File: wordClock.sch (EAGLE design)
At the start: 29 parts, among them Q1 MOSFET-PCHANNELSMD, Q2 MOSFET-PCHANNELSMD, Q3 MOSFET-PCHANNELSMD, Q4 MOSFET-PCHANNELSMD, Q5 MOSFET-PCHANNELSMD, Q6 MOSFET-PCHANNELSMD, Q7 MOSFET-PCHANNELSMD, Q8 MOSFET-PCHANNELSMD, U1 ATMEGA328P_PDIP, U2 TLC5940-NT

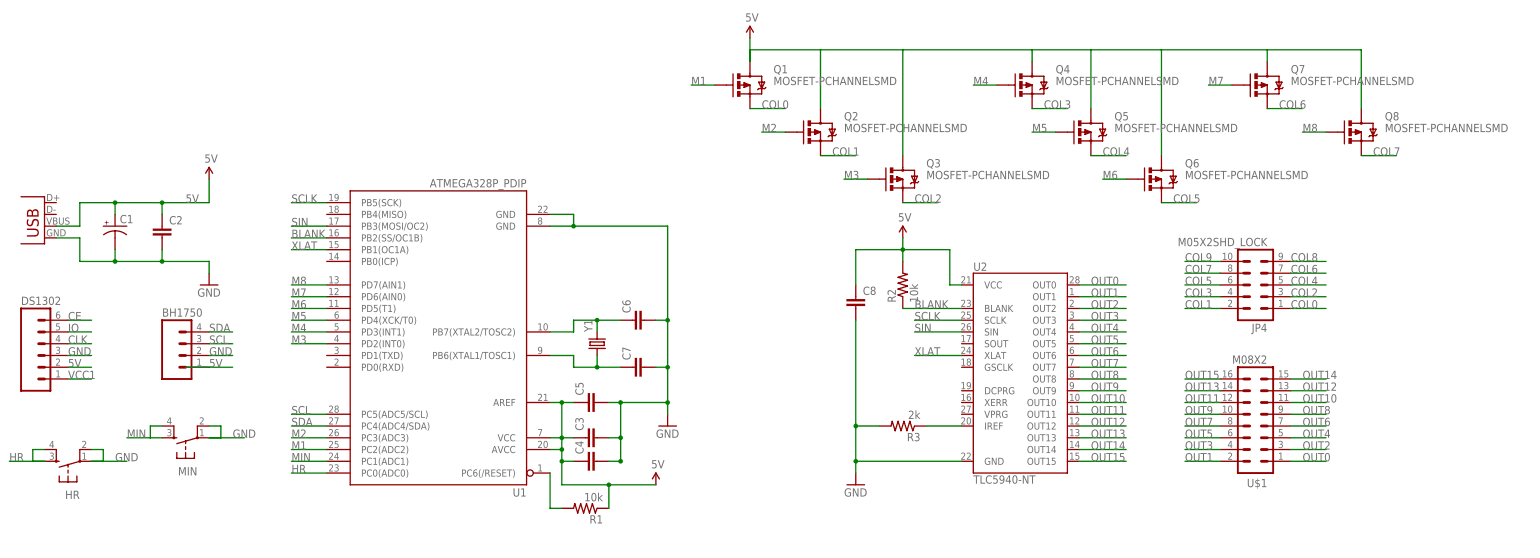
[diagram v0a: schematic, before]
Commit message: added .gitignore, change mosfet layout
Mosfets now occupy one port, for ease of programming. Mosfet D/S are now
flipped the right direction.
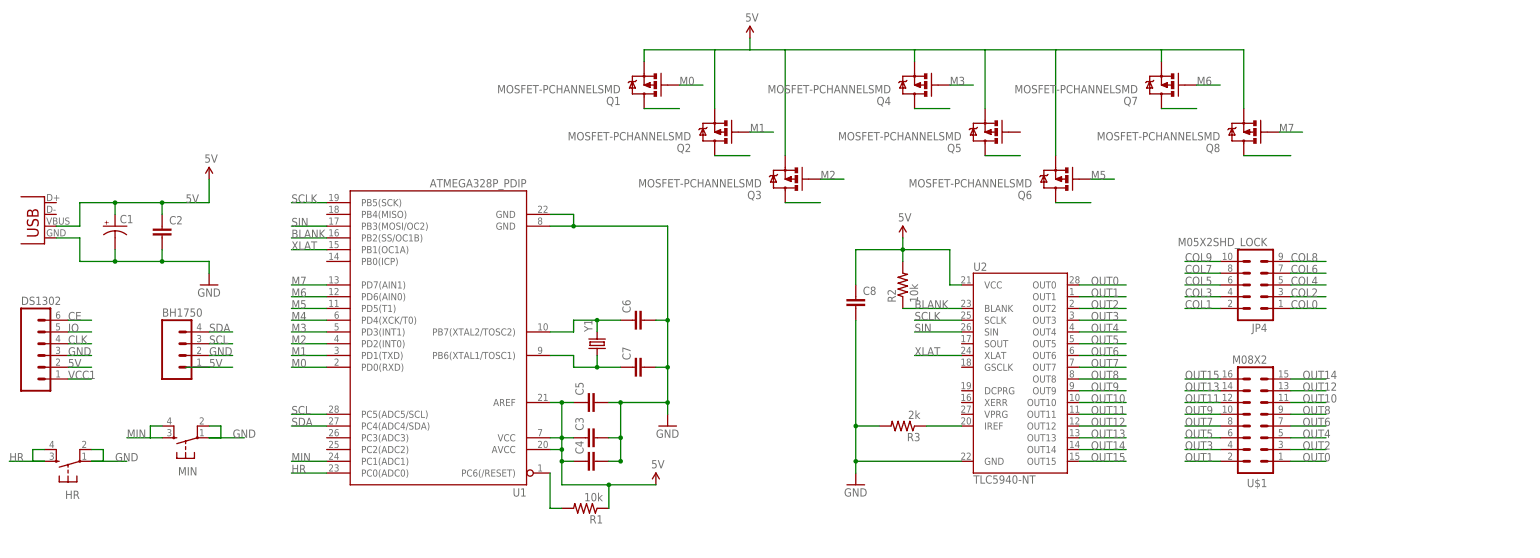
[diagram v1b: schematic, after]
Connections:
- removed net M8: Q8.G, U1.PD7(AIN1)
- new net M0: Q1.G, U1.PD0(RXD)
- new net N$10: Q6.D
- new net N$11: Q7.D
- new net N$12: Q8.D
- new net N$3: Q1.D
- new net N$6: Q2.D
- new net N$7: Q3.D
- new net N$8: Q4.D
- new net N$9: Q5.D
- net 5V: now also Q1.S, Q2.S, Q3.S, Q4.S, Q5.S, Q6.S, Q7.S, Q8.S; no longer Q1.D, Q2.D, Q3.D, Q4.D, Q5.D, Q6.D, Q7.D, Q8.D
- net COL0: no longer Q1.S
- net COL1: no longer Q2.S
- net COL2: no longer Q3.S
- net COL3: no longer Q4.S
- net COL4: no longer Q5.S
- net COL5: no longer Q6.S
- net COL6: no longer Q7.S
- net COL7: no longer Q8.S
- net M1: now also Q2.G, U1.PD1(TXD); no longer Q1.G, U1.PC2(ADC2)
- net M2: now also Q3.G, U1.PD2(INT0); no longer Q2.G, U1.PC3(ADC3)
- net M3: now also Q4.G, U1.PD3(INT1); no longer Q3.G, U1.PD2(INT0)
- net M4: now also U1.PD4(XCK/T0); no longer Q4.G, U1.PD3(INT1)
- net M5: now also Q6.G, U1.PD5(T1); no longer Q5.G, U1.PD4(XCK/T0)
- net M6: now also Q7.G, U1.PD6(AIN0); no longer Q6.G, U1.PD5(T1)
- net M7: now also Q8.G, U1.PD7(AIN1); no longer Q7.G, U1.PD6(AIN0)
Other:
- moved on the sheet: Q1, Q2, Q3, Q4, Q5, Q6, Q7, Q8

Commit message: Added AVR ISP programming header
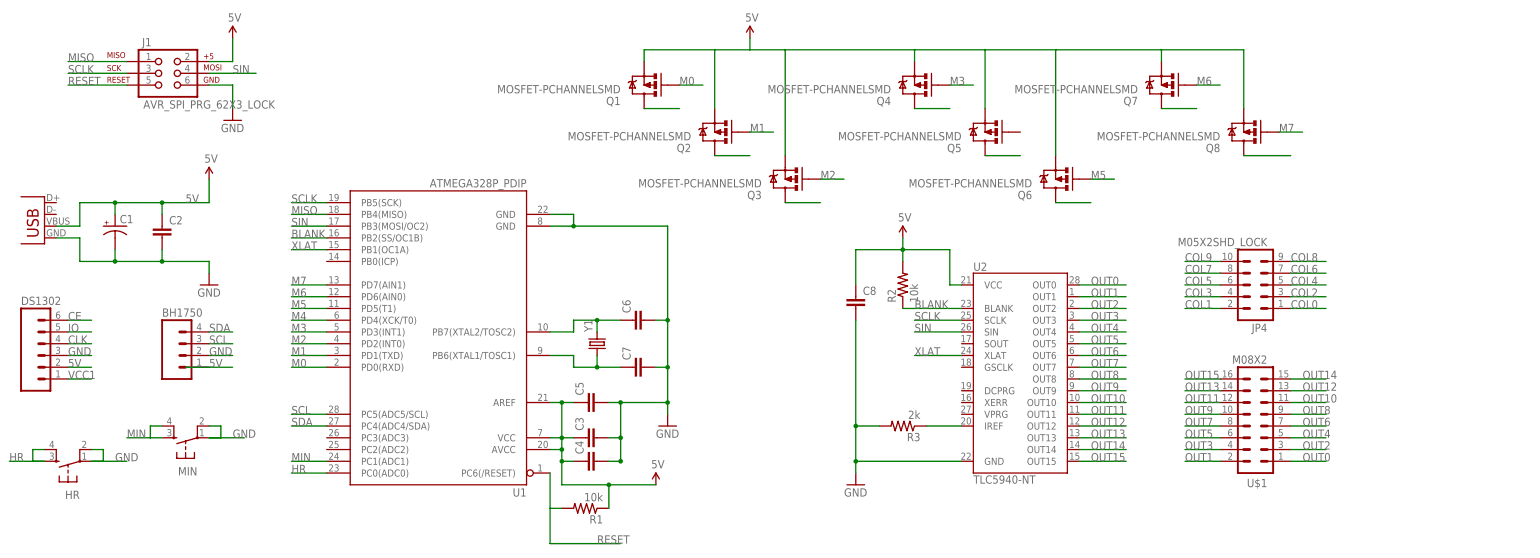
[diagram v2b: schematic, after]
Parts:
- added J1: AVR_SPI_PRG_62X3_LOCK, SparkFun-Connectors:AVR_SPI_PRG_62X3_LOCK
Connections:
- removed net N$5: R1.2, U1.PC6(/RESET)
- new net MISO: J1.1, U1.PB4(MISO)
- new net RESET: J1.5, R1.2, U1.PC6(/RESET)
- net 5V: now also J1.2
- net GND: now also J1.6
- net SCLK: now also J1.3
- net SIN: now also J1.4
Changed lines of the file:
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@@
 <part name="R3" library="SparkFun-Passives" deviceset="RESISTOR" device="0805-RES" value="2k"/>
 <part name="GND3" library="SparkFun-Aesthetics" deviceset="GND" device=""/>
+<part name="J1" library="SparkFun-Connectors" deviceset="AVR_SPI_PRG_6" device="2X3_LOCK"/>
+<part name="SUPPLY5" library="SparkFun-Aesthetics" deviceset="5V" device=""/>
+<part name="GND4" library="SparkFun-Aesthetics" deviceset="GND" device=""/>
 </parts>
 <sheets>
@@
 <instance part="R3" gate="G$1" x="187.96" y="25.4" rot="R180"/>
 <instance part="GND3" gate="1" x="177.8" y="12.7"/>
+<instance part="J1" gate="G$1" x="27.94" y="101.6"/>
+<instance part="SUPPLY5" gate="G$1" x="43.18" y="109.22"/>
+<instance part="GND4" gate="1" x="43.18" y="91.44"/>
 </instances>
 <busses>
@@
 <junction x="177.8" y="17.78"/>
 </segment>
+<segment>
+<pinref part="J1" gate="G$1" pin="6"/>
+<pinref part="GND4" gate="1" pin="GND"/>
+<wire x1="38.1" y1="99.06" x2="43.18" y2="99.06" width="0.1524" layer="91"/>
+<wire x1="43.18" y1="99.06" x2="43.18" y2="93.98" width="0.1524" layer="91"/>
+</segment>
 </net>
 <net name="CLK" class="0">
@@
 <label x="190.5" y="45.72" size="1.778" layer="95"/>
 </segment>
+<segment>
+<pinref part="J1" gate="G$1" pin="4"/>
+<wire x1="38.1" y1="101.6" x2="48.26" y2="101.6" width="0.1524" layer="91"/>
+<label x="43.18" y="101.6" size="1.778" layer="95"/>
+</segment>
 </net>
 <net name="SCLK" class="0">
@@
 <wire x1="200.66" y1="48.26" x2="190.5" y2="48.26" width="0.1524" layer="91"/>
 <label x="190.5" y="48.26" size="1.778" layer="95"/>
+</segment>
+<segment>
+<pinref part="J1" gate="G$1" pin="3"/>
+<wire x1="20.32" y1="101.6" x2="7.62" y2="101.6" width="0.1524" layer="91"/>
+<label x="7.62" y="101.6" size="1.778" layer="95"/>
 </segment>
 </net>
@@
 <wire x1="220.98" y1="83.82" x2="220.98" y2="106.68" width="0.1524" layer="91"/>
 </segment>
+<segment>
+<pinref part="J1" gate="G$1" pin="2"/>
+<pinref part="SUPPLY5" gate="G$1" pin="5V"/>
+<wire x1="38.1" y1="104.14" x2="43.18" y2="104.14" width="0.1524" layer="91"/>
+<wire x1="43.18" y1="104.14" x2="43.18" y2="109.22" width="0.1524" layer="91"/>
+</segment>
 </net>
 <net name="HR" class="0">
@@
 </segment>
 </net>
-<net name="N$5" class="0">
+<net name="RESET" class="0">
 <segment>
 <pinref part="U1" gate="G$1" pin="PC6(/RESET)"/>
@@
 <pinref part="R1" gate="G$1" pin="2"/>
 <wire x1="111.76" y1="7.62" x2="114.3" y2="7.62" width="0.1524" layer="91"/>
+<wire x1="111.76" y1="7.62" x2="111.76" y2="0" width="0.1524" layer="91"/>
+<wire x1="111.76" y1="0" x2="127" y2="0" width="0.1524" layer="91"/>
+<label x="121.92" y="0" size="1.778" layer="95"/>
+</segment>
+<segment>
+<pinref part="J1" gate="G$1" pin="5"/>
+<wire x1="20.32" y1="99.06" x2="7.62" y2="99.06" width="0.1524" layer="91"/>
+<label x="7.62" y="99.06" size="1.778" layer="95"/>
 </segment>
 </net>
@@
 </segment>
 </net>
+<net name="MISO" class="0">
+<segment>
+<pinref part="U1" gate="G$1" pin="PB4(MISO)"/>
+<wire x1="63.5" y1="71.12" x2="55.88" y2="71.12" width="0.1524" layer="91"/>
+<label x="55.88" y="71.12" size="1.778" layer="95"/>
+</segment>
+<segment>
+<pinref part="J1" gate="G$1" pin="1"/>
+<wire x1="20.32" y1="104.14" x2="7.62" y2="104.14" width="0.1524" layer="91"/>
+<label x="7.62" y="104.14" size="1.778" layer="95"/>
+</segment>
+</net>

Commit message: Fixed Fet to output pinout added pdf schematic
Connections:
- net COL8 renamed ROW8
- net COL9 renamed ROW9
- removed net COL0: JP4.1
- removed net COL1: JP4.2
- removed net COL2: JP4.3
- removed net COL3: JP4.4
- removed net COL4: JP4.5
- removed net COL5: JP4.6
- removed net COL6: JP4.7
- removed net COL7: JP4.8
- removed net N$10: Q6.D
- removed net N$11: Q7.D
- removed net N$12: Q8.D
- removed net N$3: Q1.D
- removed net N$6: Q2.D
- removed net N$7: Q3.D
- removed net N$8: Q4.D
- removed net N$9: Q5.D
- new net ROW0: JP4.1, Q1.D
- new net ROW1: JP4.2, Q2.D
- new net ROW2: JP4.3, Q3.D
- new net ROW3: JP4.4, Q4.D
- new net ROW4: JP4.5, Q5.D
- new net ROW5: JP4.6, Q6.D
- new net ROW6: JP4.7, Q7.D
- new net ROW7: JP4.8, Q8.D
- net M4: now also Q5.G

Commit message: updated SPI program socket, atmega, and usb package names to be a little more meaningful
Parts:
- J1: value AVR_SPI_PRG_62X3_LOCK -> SPI_PRG
- JP1: value USBPTH-VERTICAL -> USB_PWR
- U1: value ATMEGA328P_PDIP -> ATMEGA328P
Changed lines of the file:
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@@
 <?xml version="1.0" encoding="utf-8"?>
 <!DOCTYPE eagle SYSTEM "eagle.dtd">
-<eagle version="6.3">
+<eagle version="6.2">
 <drawing>
 <settings>
@@
 <grid distance="0.1" unitdist="inch" unit="inch" style="lines" multiple="1" display="no" altdistance="0.01" altunitdist="inch" altunit="inch"/>
 <layers>
-<layer number="1" name="Top" color="4" fill="1" visible="no" active="no"/>
-<layer number="2" name="Route2" color="1" fill="3" visible="no" active="no"/>
-<layer number="3" name="Route3" color="4" fill="3" visible="no" active="no"/>
-<layer number="4" name="Route4" color="1" fill="4" visible="no" active="no"/>
-<layer number="5" name="Route5" color="4" fill="4" visible="no" active="no"/>
-<layer number="6" name="Route6" color="1" fill="8" visible="no" active="no"/>
-<layer number="7" name="Route7" color="4" fill="8" visible="no" active="no"/>
-<layer number="8" name="Route8" color="1" fill="2" visible="no" active="no"/>
-<layer number="9" name="Route9" color="4" fill="2" visible="no" active="no"/>
-<layer number="10" name="Route10" color="1" fill="7" visible="no" active="no"/>
-<layer number="11" name="Route11" color="4" fill="7" visible="no" active="no"/>
-<layer number="12" name="Route12" color="1" fill="5" visible="no" active="no"/>
-<layer number="13" name="Route13" color="4" fill="5" visible="no" active="no"/>
-<layer number="14" name="Route14" color="1" fill="6" visible="no" active="no"/>
-<layer number="15" name="Route15" color="4" fill="6" visible="no" active="no"/>
-<layer number="16" name="Bottom" color="1" fill="1" visible="no" active="no"/>
-<layer number="17" name="Pads" color="2" fill="1" visible="no" active="no"/>
-<layer number="18" name="Vias" color="2" fill="1" visible="no" active="no"/>
-<layer number="19" name="Unrouted" color="6" fill="1" visible="no" active="no"/>
-<layer number="20" name="Dimension" color="15" fill="1" visible="no" active="no"/>
-<layer number="21" name="tPlace" color="16" fill="1" visible="no" active="no"/>
-<layer number="22" name="bPlace" color="7" fill="1" visible="no" active="no"/>
-<layer number="23" name="tOrigins" color="15" fill="1" visible="no" active="no"/>
-<layer number="24" name="bOrigins" color="15" fill="1" visible="no" active="no"/>
-<layer number="25" name="tNames" color="7" fill="1" visible="no" active="no"/>
-<layer number="26" name="bNames" color="7" fill="1" visible="no" active="no"/>
-<layer number="27" name="tValues" color="7" fill="1" visible="no" active="no"/>
-<layer number="28" name="bValues" color="7" fill="1" visible="no" active="no"/>
+<layer number="1" name="Top" color="4" fill="1" visible="yes" active="no"/>
+<layer number="2" name="Route2" color="1" fill="3" visible="yes" active="no"/>
+<layer number="3" name="Route3" color="4" fill="3" visible="yes" active="no"/>
+<layer number="4" name="Route4" color="1" fill="4" visible="yes" active="no"/>
+<layer number="5" name="Route5" color="4" fill="4" visible="yes" active="no"/>
+<layer number="6" name="Route6" color="1" fill="8" visible="yes" active="no"/>
+<layer number="7" name="Route7" color="4" fill="8" visible="yes" active="no"/>
+<layer number="8" name="Route8" color="1" fill="2" visible="yes" active="no"/>
+<layer number="9" name="Route9" color="4" fill="2" visible="yes" active="no"/>
+<layer number="10" name="Route10" color="1" fill="7" visible="yes" active="no"/>
+<layer number="11" name="Route11" color="4" fill="7" visible="yes" active="no"/>
+<layer number="12" name="Route12" color="1" fill="5" visible="yes" active="no"/>
+<layer number="13" name="Route13" color="4" fill="5" visible="yes" active="no"/>
+<layer number="14" name="Route14" color="1" fill="6" visible="yes" active="no"/>
+<layer number="15" name="Route15" color="4" fill="6" visible="yes" active="no"/>
+<layer number="16" name="Bottom" color="1" fill="1" visible="yes" active="no"/>
+<layer number="17" name="Pads" color="2" fill="1" visible="yes" active="no"/>
+<layer number="18" name="Vias" color="2" fill="1" visible="yes" active="no"/>
+<layer number="19" name="Unrouted" color="6" fill="1" visible="yes" active="no"/>
+<layer number="20" name="Dimension" color="15" fill="1" visible="yes" active="no"/>
+<layer number="21" name="tPlace" color="7" fill="1" visible="yes" active="no"/>
+<layer number="22" name="bPlace" color="7" fill="1" visible="yes" active="no"/>
+<layer number="23" name="tOrigins" color="15" fill="1" visible="yes" active="no"/>
+<layer number="24" name="bOrigins" color="15" fill="1" visible="yes" active="no"/>
+<layer number="25" name="tNames" color="7" fill="1" visible="yes" active="no"/>
+<layer number="26" name="bNames" color="7" fill="1" visible="yes" active="no"/>
+<layer number="27" name="tValues" color="7" fill="1" visible="yes" active="no"/>
+<layer number="28" name="bValues" color="7" fill="1" visible="yes" active="no"/>
 <layer number="29" name="tStop" color="7" fill="3" visible="no" active="no"/>
 <layer number="30" name="bStop" color="7" fill="6" visible="no" active="no"/>
@@
 <layer number="35" name="tGlue" color="7" fill="4" visible="no" active="no"/>
 <layer number="36" name="bGlue" color="7" fill="5" visible="no" active="no"/>
-<layer number="37" name="tTest" color="7" fill="1" visible="no" active="no"/>
-<layer number="38" name="bTest" color="7" fill="1" visible="no" active="no"/>
+<layer number="37" name="tTest" color="7" fill="1" visible="yes" active="no"/>
+<layer number="38" name="bTest" color="7" fill="1" visible="yes" active="no"/>
 <layer number="39" name="tKeepout" color="4" fill="11" visible="no" active="no"/>
 <layer number="40" name="bKeepout" color="1" fill="11" visible="no" active="no"/>
@@
 <layer number="44" name="Drills" color="7" fill="1" visible="no" active="no"/>
 <layer number="45" name="Holes" color="7" fill="1" visible="no" active="no"/>
-<layer number="46" name="Milling" color="3" fill="1" visible="no" active="no"/>
-<layer number="47" name="Measures" color="7" fill="1" visible="no" active="no"/>
-<layer number="48" name="Document" color="7" fill="1" visible="no" active="no"/>
-<layer number="49" name="Reference" color="7" fill="1" visible="no" active="no"/>
-<layer number="50" name="dxf" color="7" fill="1" visible="no" active="no"/>
-<layer number="51" name="tDocu" color="14" fill="1" visible="no" active="no"/>
-<layer number="52" name="bDocu" color="7" fill="1" visible="no" active="no"/>
-<layer number="53" name="tGND_GNDA" color="7" fill="9" visible="no" active="no"/>
-<layer number="54" name="bGND_GNDA" color="1" fill="9" visible="no" active="no"/>
-<layer number="56" name="wert" color="7" fill="1" visible="no" active="no"/>
+<layer number="46" name="Milling" color="3" fill="1" visible="yes" active="no"/>
+<layer number="47" name="Measures" color="7" fill="1" visible="yes" active="no"/>
+<layer number="48" name="Document" color="7" fill="1" visible="yes" active="no"/>
+<layer number="49" name="Reference" color="7" fill="1" visible="yes" active="no"/>
+<layer number="50" name="dxf" color="7" fill="1" visible="yes" active="no"/>
+<layer number="51" name="tDocu" color="7" fill="1" visible="yes" active="no"/>
+<layer number="52" name="bDocu" color="7" fill="1" visible="yes" active="no"/>
+<layer number="53" name="tGND_GNDA" color="7" fill="9" visible="yes" active="no"/>
+<layer number="54" name="bGND_GNDA" color="1" fill="9" visible="yes" active="no"/>
+<layer number="56" name="wert" color="7" fill="1" visible="yes" active="no"/>
 <layer number="91" name="Nets" color="2" fill="1" visible="yes" active="yes"/>
 <layer number="92" name="Busses" color="1" fill="1" visible="yes" active="yes"/>
@@
 </classes>
 <parts>
-<part name="JP1" library="SparkFun-Connectors" deviceset="USB" device="PTH-VERTICAL"/>
-<part name="U1" library="SparkFun-DigitalIC" deviceset="ATMEGA328P_PDIP" device=""/>
+<part name="JP1" library="SparkFun-Connectors" deviceset="USB" device="PTH-VERTICAL" value="USB_PWR"/>
+<part name="U1" library="SparkFun-DigitalIC" deviceset="ATMEGA328P_PDIP" device="" value="ATMEGA328P"/>
 <part name="HR" library="SparkFun-Electromechanical" deviceset="TAC_SWITCH" device="PTH"/>
 <part name="MIN" library="SparkFun-Electromechanical" deviceset="TAC_SWITCH" device="PTH"/>
@@
 <part name="R3" library="SparkFun-Passives" deviceset="RESISTOR" device="0805-RES" value="2k"/>
 <part name="GND3" library="SparkFun-Aesthetics" deviceset="GND" device=""/>
-<part name="J1" library="SparkFun-Connectors" deviceset="AVR_SPI_PRG_6" device="2X3_LOCK"/>
+<part name="J1" library="SparkFun-Connectors" deviceset="AVR_SPI_PRG_6" device="2X3_LOCK" value="SPI_PRG"/>
 <part name="SUPPLY5" library="SparkFun-Aesthetics" deviceset="5V" device=""/>
 <part name="GND4" library="SparkFun-Aesthetics" deviceset="GND" device=""/>
